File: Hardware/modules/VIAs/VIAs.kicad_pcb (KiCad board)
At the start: 4 copper layers, 83.3 x 68.2 mm, 14 parts, among them J1 Bus_PCI_6502, J2 Port 1, J3 Port 2, U1 W65C22SxP, U2 W65C22SxP, U3 74HC138

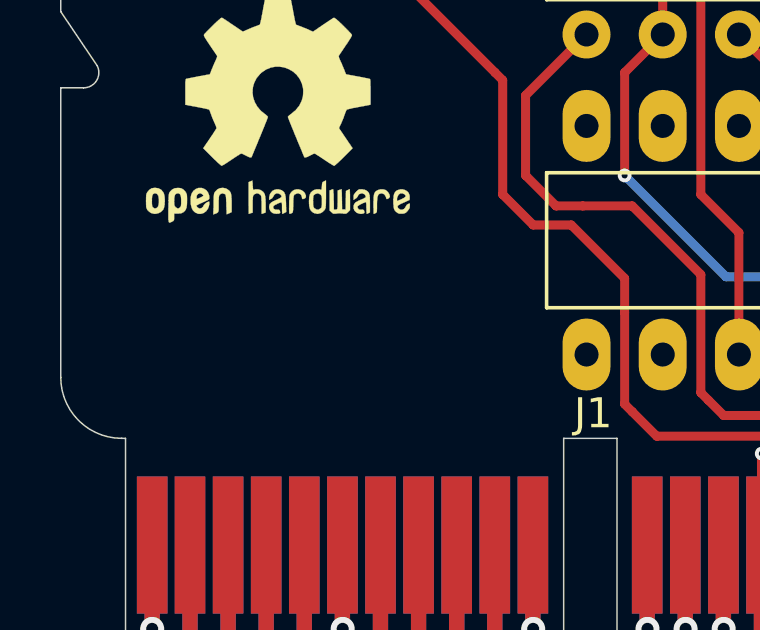
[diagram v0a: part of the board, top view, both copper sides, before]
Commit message: Hardware Review Pt. 1 fix Address Decoding for Strobe Generators add bulk capacitance to every board fix wiring of Prototyping Board
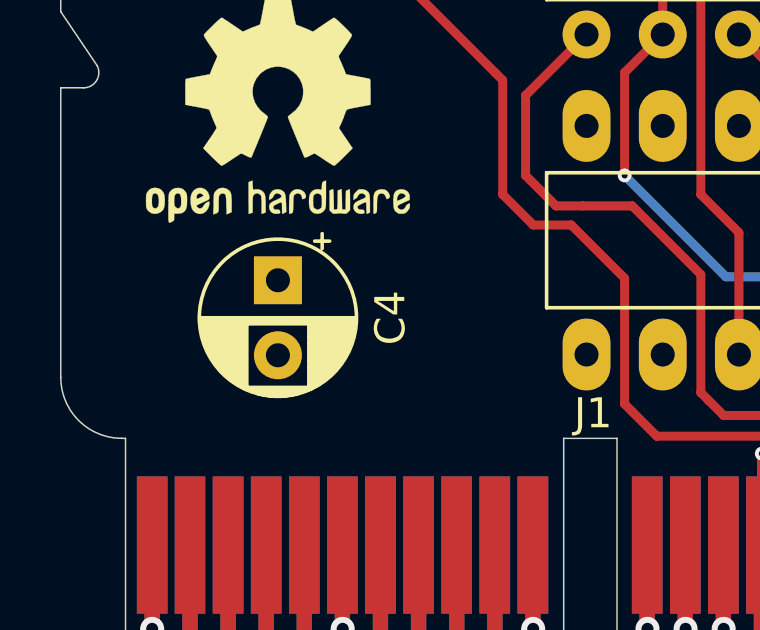
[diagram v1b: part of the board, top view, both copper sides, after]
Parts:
- added C4: 10µ, Capacitor_THT:CP_Radial_D5.0mm_P2.50mm, F.Cu at (109.9, 126.3)
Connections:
- J1 pad A11: /A13 -> unconnected-(J1-A13-PadA11)_0
- J1 pad A12: /A15 -> unconnected-(J1-A15-PadA12)
- J1 pad A25: /~{ROM} -> unconnected-(J1-~{ROM}-PadA25)_0
- J1 pad A27: /~{IRQ_0.0} -> unconnected-(J1-~{IRQ_0.0}-PadA27)
- J1 pad A28: /~{IRQ_0.1} -> unconnected-(J1-~{IRQ_0.1}-PadA28)_0
- J1 pad A29: /~{IRQ_0.2} -> unconnected-(J1-~{IRQ_0.2}-PadA29)_0
- J1 pad A30: /~{IRQ_0.3} -> unconnected-(J1-~{IRQ_0.3}-PadA30)
- J1 pad A31: /~{IRQ_0.4} -> unconnected-(J1-~{IRQ_0.4}-PadA31)_0
- J1 pad A32: /~{IRQ_0.5} -> unconnected-(J1-~{IRQ_0.5}-PadA32)_0
- J1 pad A33: /~{IRQ_0.6} -> unconnected-(J1-~{IRQ_0.6}-PadA33)_0
- J1 pad A34: /~{IRQ_0.7} -> unconnected-(J1-~{IRQ_0.7}-PadA34)
- J1 pad A38: /SYNC_VPA -> unconnected-(J1-Sync/VPA-PadA38)_0
- J1 pad A39: /Ø2/VDA -> unconnected-(J1-Ø2/VDA-PadA39)_0
- J1 pad A41: /~{RDY} -> unconnected-(J1-~{RDY}-PadA41)_0
- J1 pad A42: /~{BE} -> unconnected-(J1-~{BE}-PadA42)_0
- J1 pad A45: /E -> unconnected-(J1-E-PadA45)_0
- J1 pad A53: /RAM_0 -> unconnected-(J1-RAM0-PadA53)
- J1 pad A54: /RAM_1 -> unconnected-(J1-RAM1-PadA54)_0
- J1 pad A55: /RAM_2 -> unconnected-(J1-RAM2-PadA55)
- J1 pad A56: /RAM_3 -> unconnected-(J1-RAM3-PadA56)_0
- J1 pad A58: /RAM_4 -> unconnected-(J1-RAM4-PadA58)_0
- J1 pad A59: /RAM_5 -> unconnected-(J1-RAM5-PadA59)_0
- J1 pad A60: /RAM_6 -> unconnected-(J1-RAM6-PadA60)
- J1 pad A61: /RAM_7 -> unconnected-(J1-RAM7-PadA61)_0
- J1 pad A8: /A9 -> unconnected-(J1-A9-PadA8)_0
- J1 pad A9: /A11 -> unconnected-(J1-A11-PadA9)_0
- J1 pad B11: /A12 -> unconnected-(J1-A12-PadB11)
- J1 pad B12: /A14 -> unconnected-(J1-A14-PadB12)_0
- J1 pad B24: /~{L_RAM} -> unconnected-(J1-~{L_RAM}-PadB24)
- J1 pad B25: /~{H_RAM} -> unconnected-(J1-~{H_RAM}-PadB25)_0
- J1 pad B27: /~{IRQ} -> unconnected-(J1-~{IRQ}-PadB27)
- J1 pad B28: /~{IRQ_0} -> unconnected-(J1-~{IRQ_0}-PadB28)
- J1 pad B31: /~{IRQ_3} -> unconnected-(J1-~{IRQ_3}-PadB31)
- J1 pad B32: /~{IRQ_4} -> unconnected-(J1-~{IRQ_4}-PadB32)
- J1 pad B33: /~{NMI} -> unconnected-(J1-~{NMI}-PadB33)
- J1 pad B34: /PAGE -> unconnected-(J1-PAGE_ROM-PadB34)
- J1 pad B38: /~{VP} -> unconnected-(J1-~{VP}-PadB38)_0
- J1 pad B39: /~{ML} -> unconnected-(J1-~{ML}-PadB39)_0
- J1 pad B46: /M/X -> unconnected-(J1-M/~{X}-PadB46)
- J1 pad B53: /ROM_0 -> unconnected-(J1-ROM0-PadB53)_0
- J1 pad B54: /ROM_1 -> unconnected-(J1-ROM1-PadB54)_0
- J1 pad B55: /ROM_2 -> unconnected-(J1-ROM2-PadB55)
- J1 pad B56: /ROM_3 -> unconnected-(J1-ROM3-PadB56)_0
- J1 pad B58: /ROM_4 -> unconnected-(J1-ROM4-PadB58)
- J1 pad B59: /ROM_5 -> unconnected-(J1-ROM5-PadB59)
- J1 pad B60: /ROM_6 -> unconnected-(J1-ROM6-PadB60)_0
- J1 pad B61: /ROM_7 -> unconnected-(J1-ROM7-PadB61)
- J1 pad B8: /A8 -> unconnected-(J1-A8-PadB8)_0
- J1 pad B9: /A10 -> unconnected-(J1-A10-PadB9)_0
- U3 pad 10: /PORT_80 -> unconnected-(U3-~{Y5}-Pad10)
- U3 pad 13: /PORT_32 -> unconnected-(U3-~{Y2}-Pad13)
- U3 pad 14: /PORT_16 -> unconnected-(U3-~{Y1}-Pad14)
- U3 pad 15: /PORT_0 -> unconnected-(U3-~{Y0}-Pad15)
- U3 pad 7: /PORT_112 -> unconnected-(U3-~{Y7}-Pad7)
- U3 pad 9: /PORT_96 -> unconnected-(U3-~{Y6}-Pad9)

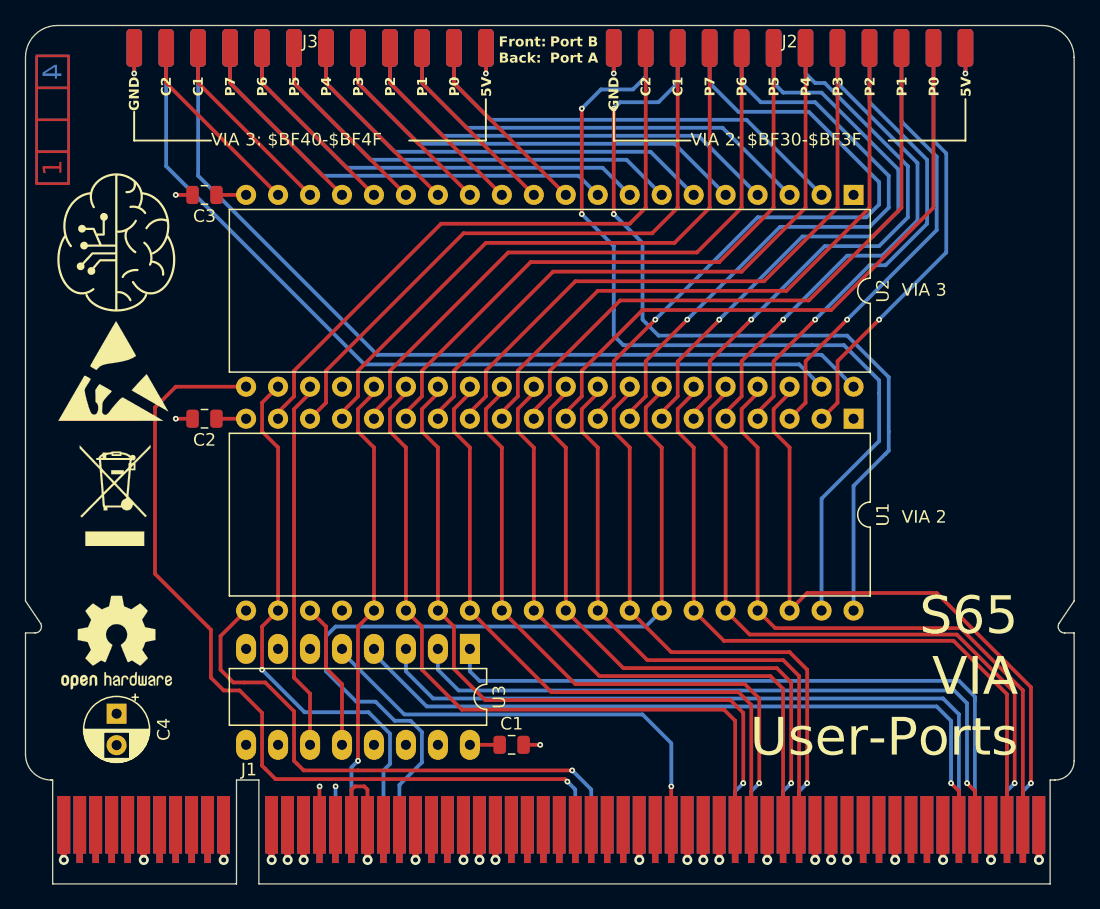
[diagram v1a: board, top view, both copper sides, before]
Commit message: Big Review Update - Changed Copper Pours on all PCBs - Implemented errors found at review - fixed some additional errors
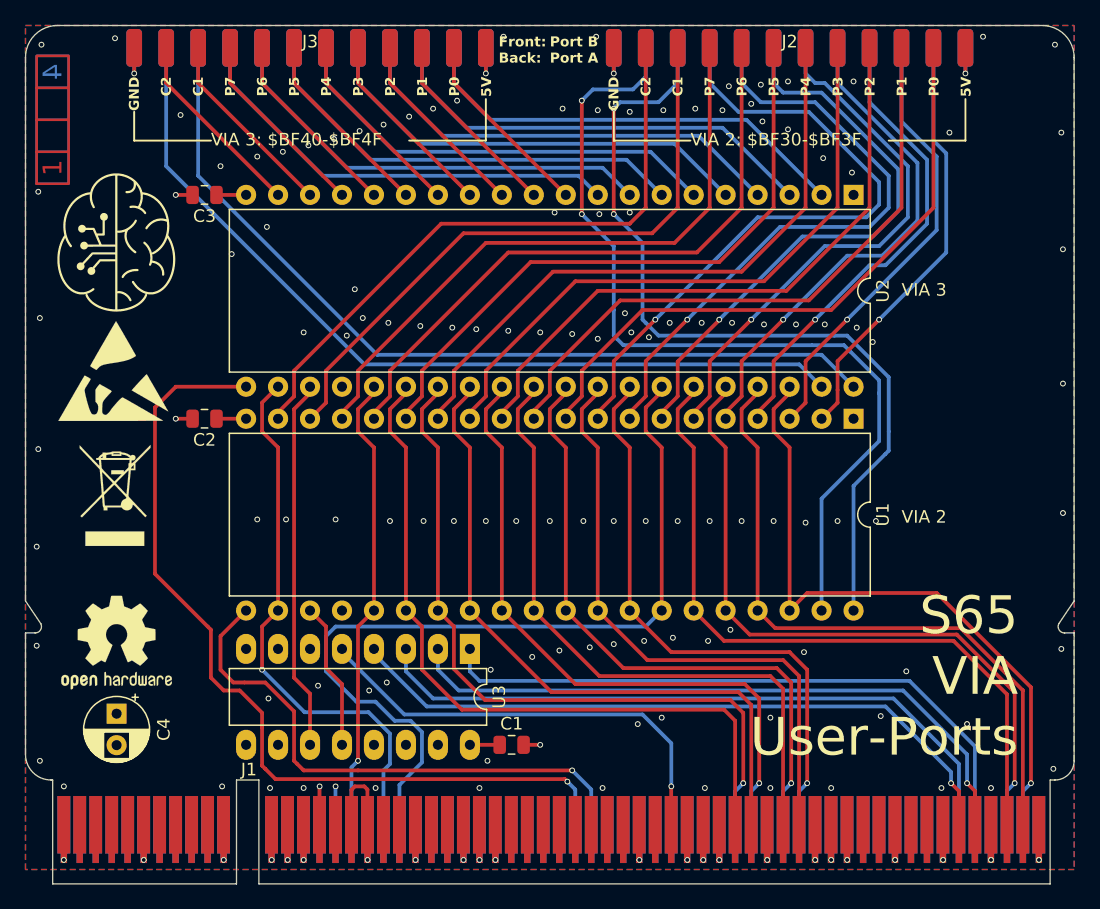
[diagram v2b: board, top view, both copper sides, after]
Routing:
- net /A7: track 57.0 -> 54.6 mm
- net /A5: track 54.7 -> 52.3 mm
- net /A4: track 52.9 -> 50.6 mm
- net /A6: track 55.9 -> 53.6 mm
- net +5V: vias 6 -> 131
- added copper zone on B.Cu, net +5V
- added copper zone on F.Cu, net +5V
- added copper zone on In1.Cu, net GND
- removed copper zone on In1.Cu, net +5V
